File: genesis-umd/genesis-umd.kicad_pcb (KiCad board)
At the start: 2 copper layers, 26.7 x 94.6 mm, 8 parts, among them CON101 UMDv2-CONN, CON102 GENESIS-CONN, U101 MCP23008T-E_SS

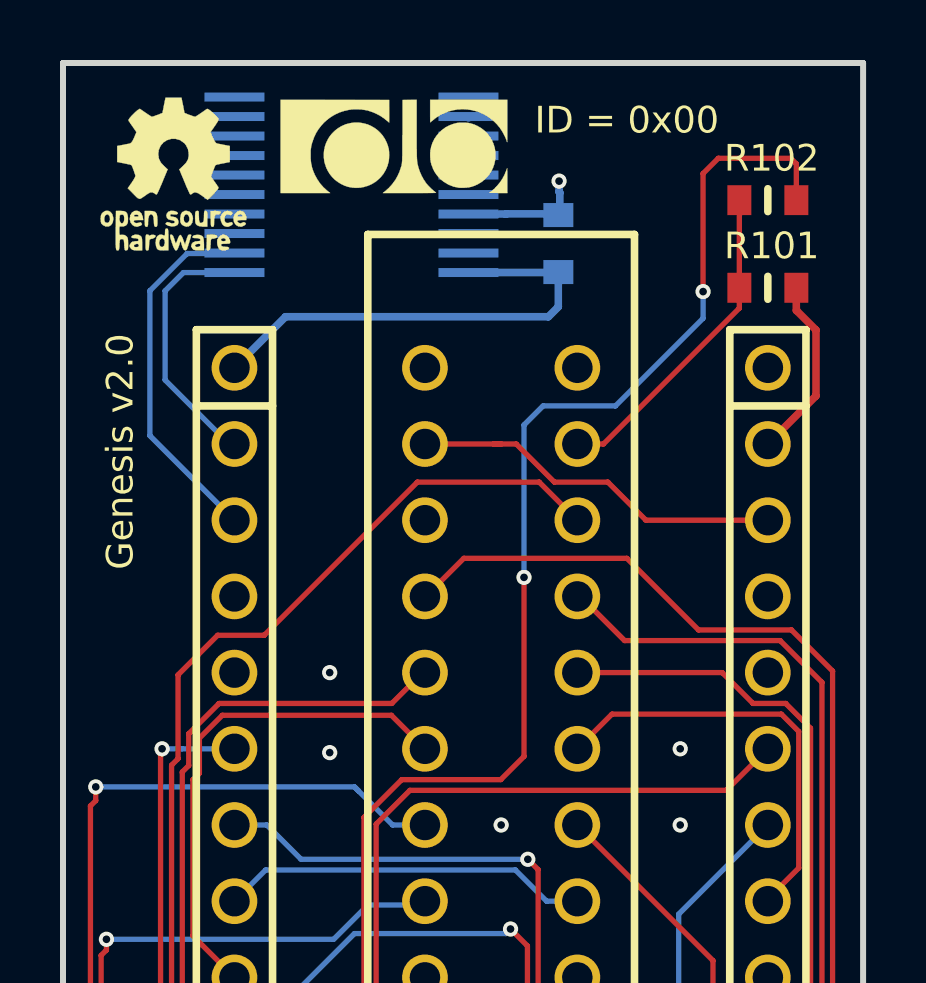
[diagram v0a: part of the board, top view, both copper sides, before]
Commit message: changed ID on board to 0x01, realized that ID 0x00 should be reserved for undefined
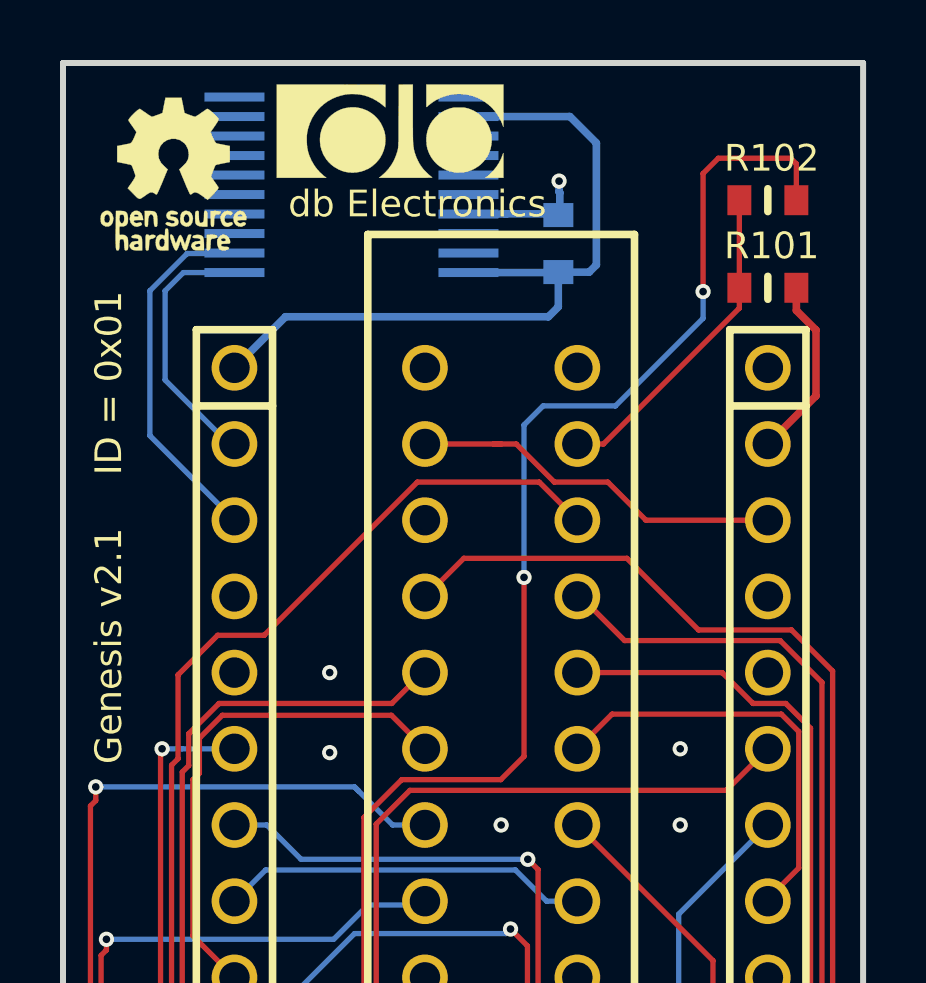
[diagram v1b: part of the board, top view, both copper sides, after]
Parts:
- moved G*** 0.52 mm to (141.1, 58.2)
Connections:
- U101 pad 12: GND -> +3V3
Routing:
- net +3V3: track 15.8 -> 25.9 mm
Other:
- board text added: "Genesis v2.1"
- board text added: "ID = 0x01"
- board text added: "db Electronics"
- board text removed: "Genesis v2.0"
- board text removed: "ID = 0x00"
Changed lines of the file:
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@@
   (general
     (thickness 1.6)
-    (drawings 9)
-    (tracks 523)
+    (drawings 10)
+    (tracks 528)
     (zones 0)
     (modules 8)
@@
   (title_block
     (title "Sega Genesis UMDv2 Adapter")
-    (date 2020-02-10)
-    (rev 2.0)
+    (date 2020-02-12)
+    (rev 2.1)
     (company "db Electronics")
     (comment 1 "Licensed Under CERN OHL v.1.2")
-    (comment 2 https://github.com/db-electronics/UMDv2-kicad)
+    (comment 2 https://github.com/db-electronics/UMDv2-genesis-kicad)
   )
   (layers
@@
       (drillshape 0)
       (scaleselection 1)
-      (outputdirectory "gerbers/2.0/"))
+      (outputdirectory "gerbers/2.1/"))
   )
   (net 0 "")
@@
     (add_net GND)
   )
-  (module db-smt:0603 (layer F.Cu)
-    (at 153.67 60.452)
-    (tags 0603)
-    (solder_mask_margin 0.1016)
-    (attr smd)
-    (fp_text reference R102 (at 0.127 -1.397) (layer F.SilkS)
-      (effects (font (size 0.889 0.889) (thickness 0.2032)))
-    )
-    (fp_text value 0 (at 0.508 -2.54) (layer F.Fab) hide
-      (effects (font (size 1 1) (thickness 0.15)))
-    )
-    (fp_line (start 0 -0.381) (end 0 0.381) (layer F.SilkS) (width 0.254))
-    (pad 2 smd rect (at 0.95 0) (size 0.8 1) (layers F.Cu F.Paste F.Mask)
-      (net 10 /~WR~))
-    (pad 1 smd rect (at -0.95 0) (size 0.8 1) (layers F.Cu F.Paste F.Mask)
-      (net 58 "Net-(CON102-PadA2)"))
-    (model Resistors_SMD.3dshapes/R_0603.wrl
-      (at (xyz 0 0 0))
-      (scale (xyz 1 1 1))
-      (rotate (xyz 0 0 0))
-    )
-  )
-  (module db-smt:0603 (layer F.Cu)
-    (at 153.67 63.373)
-    (tags 0603)
-    (solder_mask_margin 0.1016)
-    (attr smd)
-    (fp_text reference R101 (at 0.127 -1.397) (layer F.SilkS)
-      (effects (font (size 0.889 0.889) (thickness 0.2032)))
-    )
-    (fp_text value 0 (at 0.508 -2.54) (layer F.Fab) hide
-      (effects (font (size 1 1) (thickness 0.15)))
-    )
-    (fp_line (start 0 -0.381) (end 0 0.381) (layer F.SilkS) (width 0.254))
-    (pad 2 smd rect (at 0.95 0) (size 0.8 1) (layers F.Cu F.Paste F.Mask)
-      (net 56 /5V_0))
-    (pad 1 smd rect (at -0.95 0) (size 0.8 1) (layers F.Cu F.Paste F.Mask)
-      (net 58 "Net-(CON102-PadA2)"))
-    (model Resistors_SMD.3dshapes/R_0603.wrl
-      (at (xyz 0 0 0))
-      (scale (xyz 1 1 1))
-      (rotate (xyz 0 0 0))
-    )
-  )
   (module db-artwork:db-logo_7.5mm (layer F.Cu)
-    (at 141.224 58.674)
+    (at 141.097 58.166)
     (fp_text reference G*** (at 0 0) (layer F.SilkS) hide
       (effects (font (size 1.524 1.524) (thickness 0.3)))
@@
       (xy -2.473934 1.22547) (xy -2.375576 1.338595) (xy -2.263359 1.444092) (xy -2.210097 1.487916)
       (xy -2.142804 1.54122) (xy -3.797084 1.54122) (xy -3.797084 -1.567091) (xy -1.986796 -1.564919)) (layer F.SilkS) (width 0.01))
+  )
+  (module db-smt:0603 (layer F.Cu)
+    (at 153.67 60.452)
+    (tags 0603)
+    (solder_mask_margin 0.1016)
+    (attr smd)
+    (fp_text reference R102 (at 0.127 -1.397) (layer F.SilkS)
+      (effects (font (size 0.889 0.889) (thickness 0.2032)))
+    )
+    (fp_text value 0 (at 0.508 -2.54) (layer F.Fab) hide
+      (effects (font (size 1 1) (thickness 0.15)))
+    )
+    (fp_line (start 0 -0.381) (end 0 0.381) (layer F.SilkS) (width 0.254))
+    (pad 2 smd rect (at 0.95 0) (size 0.8 1) (layers F.Cu F.Paste F.Mask)
+      (net 10 /~WR~))
+    (pad 1 smd rect (at -0.95 0) (size 0.8 1) (layers F.Cu F.Paste F.Mask)
+      (net 58 "Net-(CON102-PadA2)"))
+    (model Resistors_SMD.3dshapes/R_0603.wrl
+      (at (xyz 0 0 0))
+      (scale (xyz 1 1 1))
+      (rotate (xyz 0 0 0))
+    )
+  )
+  (module db-smt:0603 (layer F.Cu)
+    (at 153.67 63.373)
+    (tags 0603)
+    (solder_mask_margin 0.1016)
+    (attr smd)
+    (fp_text reference R101 (at 0.127 -1.397) (layer F.SilkS)
+      (effects (font (size 0.889 0.889) (thickness 0.2032)))
+    )
+    (fp_text value 0 (at 0.508 -2.54) (layer F.Fab) hide
+      (effects (font (size 1 1) (thickness 0.15)))
+    )
+    (fp_line (start 0 -0.381) (end 0 0.381) (layer F.SilkS) (width 0.254))
+    (pad 2 smd rect (at 0.95 0) (size 0.8 1) (layers F.Cu F.Paste F.Mask)
+      (net 56 /5V_0))
+    (pad 1 smd rect (at -0.95 0) (size 0.8 1) (layers F.Cu F.Paste F.Mask)
+      (net 58 "Net-(CON102-PadA2)"))
+    (model Resistors_SMD.3dshapes/R_0603.wrl
+      (at (xyz 0 0 0))
+      (scale (xyz 1 1 1))
+      (rotate (xyz 0 0 0))
+    )
   )
   (module db-artwork:oshw-logo_5mm (layer F.Cu)
@@
     (solder_mask_margin 0.1016)
     (attr smd)
-    (fp_text reference C101 (at 0 1.905 90) (layer B.SilkS)
+    (fp_text reference C101 (at 0 1.524 90) (layer B.SilkS)
       (effects (font (size 0.889 0.889) (thickness 0.2032)) (justify mirror))
     )
@@
     (at 135.89 62.865)
     (solder_mask_margin 0.1)
-    (fp_text reference U101 (at 4.445 1.27) (layer B.SilkS)
+    (fp_text reference U101 (at 4.953 1.27) (layer B.SilkS)
       (effects (font (size 0.889 0.889) (thickness 0.2032)) (justify mirror))
     )
@@
     (pad 11 smd rect (at 7.8 -5.85) (size 2 0.3) (layers B.Cu B.Paste B.Mask))
     (pad 12 smd rect (at 7.8 -5.2) (size 2 0.3) (layers B.Cu B.Paste B.Mask)
-      (net 2 GND))
+      (net 1 +3V3))
     (pad 13 smd rect (at 7.8 -4.55) (size 2 0.3) (layers B.Cu B.Paste B.Mask)
       (net 2 GND))
@@
     (pad 18 smd rect (at 7.8 -1.3) (size 2 0.3) (layers B.Cu B.Paste B.Mask)
       (net 2 GND))
+  )
+  (gr_text "db Electronics" (at 141.986 60.579) (layer F.SilkS)
+    (effects (font (size 0.889 0.889) (thickness 0.1524)))
   )
   (dimension 94.615 (width 0.15) (layer Dwgs.User)
@@
     (arrow2b (pts (xy 156.845 152.908) (xy 155.718496 153.494421)))
   )
-  (gr_text "ID = 0x00" (at 148.971 57.785) (layer F.SilkS)
+  (gr_text "ID = 0x01" (at 131.699 66.548 90) (layer F.SilkS)
     (effects (font (size 0.889 0.889) (thickness 0.1524)))
   )
-  (gr_text "Genesis v2.0" (at 132.08 68.834 90) (layer F.SilkS)
+  (gr_text "Genesis v2.1" (at 131.699 75.311 90) (layer F.SilkS)
     (effects (font (size 0.889 0.889) (thickness 0.1524)))
   )
@@
   (segment (start 146.6698 62.865) (end 146.685 62.8498) (width 0.254) (layer B.Cu) (net 1) (status 30))
   (segment (start 143.69 62.865) (end 146.6698 62.865) (width 0.254) (layer B.Cu) (net 1) (status 30))
+  (segment (start 143.69 57.711) (end 143.6878 57.7088) (width 0.254) (layer B.Cu) (net 1))
+  (segment (start 143.69 57.665) (end 147.073 57.665) (width 0.254) (layer B.Cu) (net 1))
+  (segment (start 147.073 57.665) (end 147.955 58.547) (width 0.254) (layer B.Cu) (net 1))
+  (segment (start 147.955 58.547) (end 147.955 62.611) (width 0.254) (layer B.Cu) (net 1))
+  (segment (start 147.7162 62.8498) (end 146.685 62.8498) (width 0.254) (layer B.Cu) (net 1))
+  (segment (start 147.955 62.611) (end 147.7162 62.8498) (width 0.254) (layer B.Cu) (net 1))
   (via (at 146.7104 59.817) (size 0.508) (drill 0.254) (layers F.Cu B.Cu) (net 2))
   (segment (start 146.7104 60.17621) (end 146.7358 60.20161) (width 0.254) (layer B.Cu) (net 2))
@@
   (segment (start 144.9498 60.9092) (end 146.6342 60.9092) (width 0.254) (layer B.Cu) (net 2))
   (segment (start 146.6342 60.9092) (end 146.6596 60.8838) (width 0.254) (layer B.Cu) (net 2))
-  (segment (start 143.69 57.711) (end 143.6878 57.7088) (width 0.254) (layer B.Cu) (net 2))
   (via (at 139.065 76.2) (size 0.508) (drill 0.254) (layers F.Cu B.Cu) (net 2))
   (via (at 139.065 78.867) (size 0.508) (drill 0.254) (layers F.Cu B.Cu) (net 2))

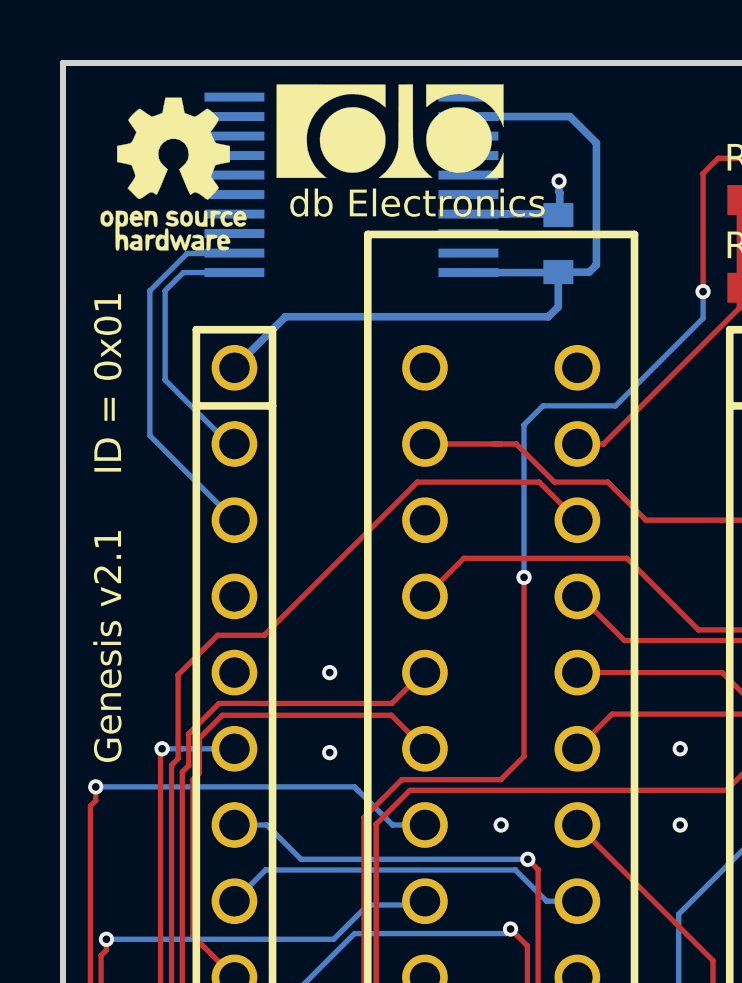
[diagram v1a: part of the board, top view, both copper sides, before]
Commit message: corrected nRST tied permanently low on MCP23008
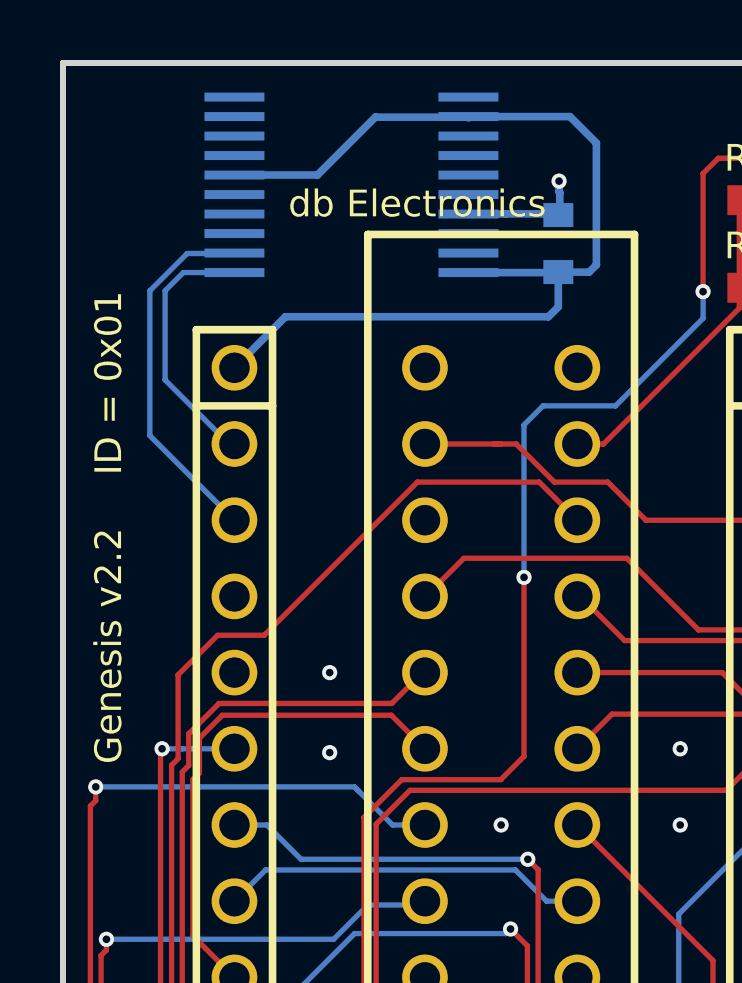
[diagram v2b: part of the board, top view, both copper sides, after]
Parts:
- removed G***: LOGO, db-artwork:db-logo_7.5mm
- removed G***: LOGO, db-artwork:oshw-logo_5mm
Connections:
- CON101 pad 25: (no net) -> Net-(CON101-Pad25)
- CON101 pad 36: (no net) -> /A0
- CON101 pad 4: (no net) -> Net-(CON101-Pad4)
- CON101 pad 40: (no net) -> Net-(CON101-Pad40)
- CON101 pad 5: (no net) -> Net-(CON101-Pad5)
- CON101 pad 60: (no net) -> Net-(CON101-Pad60)
- CON101 pad 61: (no net) -> Net-(CON101-Pad61)
- CON101 pad 65: (no net) -> Net-(CON101-Pad65)
- CON101 pad 66: (no net) -> Net-(CON101-Pad66)
- CON102 pad B1: (no net) -> Net-(CON102-PadB1)
- CON102 pad B12: (no net) -> Net-(CON102-PadB12)
- CON102 pad B13: (no net) -> Net-(CON102-PadB13)
- CON102 pad B14: (no net) -> Net-(CON102-PadB14)
- CON102 pad B15: (no net) -> Net-(CON102-PadB15)
- CON102 pad B19: (no net) -> Net-(CON102-PadB19)
- CON102 pad B21: (no net) -> Net-(CON102-PadB21)
- CON102 pad B3: (no net) -> Net-(CON102-PadB3)
- U101 pad 10: (no net) -> Net-(U101-Pad10)
- U101 pad 11: (no net) -> Net-(U101-Pad11)
- U101 pad 6: GND -> +3V3
- U101 pad 7: (no net) -> Net-(U101-Pad7)
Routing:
- net +3V3: track 25.9 -> 34.5 mm
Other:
- board text added: "Genesis v2.2"
- board text removed: "Genesis v2.1"

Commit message: added OSHWA markings for v2.2 release
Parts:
- added G***: LOGO, db-artwork:oshw-logo_5mm, F.Cu at (133.8, 59.3)
- added G***: LOGO, db-artwork:db-logo_7.5mm, F.Cu at (141.0, 58.2)
